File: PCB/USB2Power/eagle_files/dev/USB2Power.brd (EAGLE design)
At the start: 12.5 x 20 mm, 7 parts, among them SW1 PCM12SMTR

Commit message: USB2Power board components placed and ready for routing.
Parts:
- moved SW1 7.02 mm to (2.00, 8.50), flipped to the top, turned to 270 degrees
- moved C1 6.92 mm to (7.99, 4.50), flipped to the bottom, turned to 180 degrees
- moved C2 4.63 mm to (5.00, 11.0), flipped to the bottom, turned to 270 degrees
- moved USB1 4.51 mm to (8.50, 2.25)
- moved JP1 3.25 mm to (2.00, 14.8)
- moved L1 2.64 mm to (7.75, 11.2), flipped to the bottom
- moved VR1 2.20 mm to (7.25, 7.50), flipped to the bottom
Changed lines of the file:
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@@
 </autorouter>
 <elements>
-<element name="C1" library="SparkFun-Capacitors" package="0603-CAP" value="" x="1.75" y="7.5" smashed="yes" rot="R270">
-<attribute name="NAME" x="2.531" y="9.442" size="0.4064" layer="25" font="vector"/>
-<attribute name="VALUE" x="0.607" y="8.516" size="0.4064" layer="27" font="vector" rot="R270"/>
+<element name="C1" library="SparkFun-Capacitors" package="0603-CAP" value="" x="7.99" y="4.5" smashed="yes" rot="MR180">
+<attribute name="NAME" x="5.711" y="3.318" size="0.4064" layer="26" font="vector" rot="MR180"/>
+<attribute name="VALUE" x="6.974" y="5.643" size="0.4064" layer="28" font="vector" rot="MR180"/>
 </element>
-<element name="C2" library="SparkFun-Capacitors" package="0603-CAP" value="" x="2.53" y="14.92" smashed="yes">
-<attribute name="NAME" x="0.721" y="13.252" size="0.4064" layer="25" font="vector"/>
-<attribute name="VALUE" x="1.514" y="13.777" size="0.4064" layer="27" font="vector"/>
+<element name="C2" library="SparkFun-Capacitors" package="0603-CAP" value="" x="5" y="11" smashed="yes" rot="MR270">
+<attribute name="NAME" x="4.021" y="13.058" size="0.4064" layer="26" font="vector" rot="MR180"/>
+<attribute name="VALUE" x="6.143" y="12.016" size="0.4064" layer="28" font="vector" rot="MR270"/>
 </element>
-<element name="JP1" library="SparkFun-Connectors" package="1X04" value="" x="2" y="18" smashed="yes">
-<attribute name="NAME" x="9.5038" y="14.7588" size="1.27" layer="25" ratio="10"/>
-<attribute name="VALUE" x="0.73" y="14.825" size="1.27" layer="27"/>
+<element name="JP1" library="SparkFun-Connectors" package="1X04" value="" x="2" y="14.75" smashed="yes">
+<attribute name="NAME" x="8.4538" y="11.7588" size="1.27" layer="25" ratio="10"/>
+<attribute name="VALUE" x="0.73" y="11.575" size="1.27" layer="27"/>
 </element>
-<element name="L1" library="SparkFun-Passives" package="0603" value="" x="5.37" y="12.39" smashed="yes">
-<attribute name="PROD_ID" value="RES-07859" x="5.37" y="12.39" size="1.778" layer="27" display="off"/>
-<attribute name="NAME" x="7.191" y="12.442" size="0.4064" layer="25" font="vector"/>
-<attribute name="VALUE" x="4.354" y="11.247" size="0.4064" layer="27" font="vector"/>
+<element name="L1" library="SparkFun-Passives" package="0603" value="" x="7.75" y="11.25" smashed="yes" rot="MR0">
+<attribute name="PROD_ID" value="RES-07859" x="7.75" y="11.25" size="1.778" layer="28" rot="MR0" display="off"/>
+<attribute name="NAME" x="8.809" y="12.452" size="0.4064" layer="26" font="vector" rot="MR0"/>
+<attribute name="VALUE" x="8.766" y="10.107" size="0.4064" layer="28" font="vector" rot="MR0"/>
 </element>
-<element name="SW1" library="freddyLibr" package="PCM12SMTR" value="PCM12SMTR" x="4.67" y="2.01" smashed="yes" rot="MR0">
-<attribute name="NAME" x="6.24" y="5.13" size="1.27" layer="26" rot="MR0"/>
+<element name="SW1" library="freddyLibr" package="PCM12SMTR" value="PCM12SMTR" x="2" y="8.5" smashed="yes" rot="R270">
+<attribute name="NAME" x="0.53" y="2.72" size="1.27" layer="25"/>
 </element>
-<element name="USB1" library="freddyLibr" package="USB-MICROB-SMT" value="USB-MICROB-SMT5-PIN" x="4" y="2.5" smashed="yes">
-<attribute name="NAME" x="11.35" y="6.14" size="1.27" layer="25" rot="R180"/>
+<element name="USB1" library="freddyLibr" package="USB-MICROB-SMT" value="USB-MICROB-SMT5-PIN" x="8.5" y="2.25" smashed="yes">
+<attribute name="NAME" x="0.64" y="0.48" size="1.27" layer="25"/>
 </element>
-<element name="VR1" library="freddyLibr" package="UJ-5_TSOT" value="" x="5.3" y="8.51" smashed="yes">
-<attribute name="NAME" x="7.63" y="9.02" size="1.27" layer="25"/>
+<element name="VR1" library="freddyLibr" package="UJ-5_TSOT" value="" x="7.25" y="7.5" smashed="yes" rot="MR0">
+<attribute name="NAME" x="5.59" y="7.72" size="1.27" layer="26" rot="MR0"/>
 </element>
 </elements>
@@
 <contactref element="VR1" pad="3"/>
 <contactref element="C1" pad="2"/>
-<wire x1="6.25" y1="7.36" x2="2.42" y2="3.76" width="0" layer="19" extent="1-1"/>
-<wire x1="4.35" y1="7.36" x2="6.25" y2="7.36" width="0" layer="19" extent="1-1"/>
-<wire x1="1.75" y1="6.65" x2="4.35" y2="7.36" width="0" layer="19" extent="1-1"/>
+<wire x1="8.2" y1="6.35" x2="6.3" y2="6.35" width="0" layer="19" extent="1-1"/>
+<wire x1="8.84" y1="4.5" x2="8.2" y2="6.35" width="0" layer="19" extent="1-1"/>
+<wire x1="3.75" y1="6.25" x2="6.3" y2="6.35" width="0" layer="19" extent="1-16"/>
 </signal>
 <signal name="N$2">
 <contactref element="VR1" pad="4"/>
 <contactref element="L1" pad="1"/>
-<wire x1="4.52" y1="12.39" x2="4.35" y2="9.66" width="0" layer="19" extent="1-1"/>
+<wire x1="8.2" y1="8.65" x2="8.6" y2="11.25" width="0" layer="19" extent="1-16"/>
 </signal>
 <signal name="GND">
@@
 <contactref element="USB1" pad="9"/>
 <contactref element="JP1" pad="1"/>
-<wire x1="5.3" y1="7.36" x2="5.3" y2="4.13" width="0" layer="19" extent="1-1"/>
-<wire x1="2" y1="18" x2="5.3" y2="7.36" width="0" layer="19" extent="1-1"/>
-<wire x1="1.68" y1="14.92" x2="2" y2="18" width="0" layer="19" extent="1-1"/>
-<wire x1="1.75" y1="8.35" x2="1.68" y2="14.92" width="0" layer="19" extent="1-1"/>
+<wire x1="5" y1="11.85" x2="2" y2="14.75" width="0" layer="19" extent="16-16"/>
+<wire x1="7.14" y1="4.5" x2="5" y2="11.85" width="0" layer="19" extent="1-16"/>
+<wire x1="7.25" y1="6.35" x2="7.14" y2="4.5" width="0" layer="19" extent="1-1"/>
+<wire x1="9.8" y1="3.88" x2="7.25" y2="6.35" width="0" layer="19" extent="1-1"/>
 </signal>
 <signal name="VIN">
 <contactref element="USB1" pad="5"/>
 <contactref element="SW1" pad="2"/>
-<wire x1="3.92" y1="3.76" x2="2.7" y2="4.13" width="0" layer="19" extent="1-1"/>
+<wire x1="7.2" y1="3.88" x2="3.75" y2="7.75" width="0" layer="19" extent="1-16"/>
 </signal>
 <signal name="VOUT">
@@
 <contactref element="SW1" pad="1"/>
 <contactref element="JP1" pad="2"/>
-<wire x1="6.22" y1="12.39" x2="3.38" y2="14.92" width="0" layer="19" extent="1-1"/>
-<wire x1="4.54" y1="18" x2="6.22" y2="12.39" width="0" layer="19" extent="1-1"/>
-<wire x1="6.92" y1="3.76" x2="4.54" y2="18" width="0" layer="19" extent="1-1"/>
-<wire x1="6.25" y1="9.66" x2="6.22" y2="12.39" width="0" layer="19" extent="1-1"/>
+<wire x1="6.3" y1="8.65" x2="6.9" y2="11.25" width="0" layer="19" extent="1-16"/>
+<wire x1="4.54" y1="14.75" x2="6.9" y2="11.25" width="0" layer="19" extent="16-16"/>
+<wire x1="5" y1="10.15" x2="6.3" y2="8.65" width="0" layer="19" extent="1-16"/>
+<wire x1="3.75" y1="10.75" x2="5" y2="10.15" width="0" layer="19" extent="16-16"/>
 </signal>
 </signals>

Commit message: Slightly tweak borders of USB2Power.
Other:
- board size 12.5 x 20 mm -> 12.5 x 16.5 mm
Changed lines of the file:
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@@
 <plain>
 <wire x1="0" y1="0" x2="12.5" y2="0" width="0" layer="20"/>
-<wire x1="12.5" y1="0" x2="12.52" y2="20" width="0" layer="20"/>
-<wire x1="12.52" y1="20" x2="0" y2="20" width="0" layer="20"/>
-<wire x1="0" y1="20" x2="0" y2="0" width="0" layer="20"/>
+<wire x1="12.5" y1="0" x2="12.5" y2="16.5" width="0" layer="20"/>
+<wire x1="12.5" y1="16.5" x2="0" y2="16.5" width="0" layer="20"/>
+<wire x1="0" y1="16.5" x2="0" y2="0" width="0" layer="20"/>
 </plain>
 <attributes>

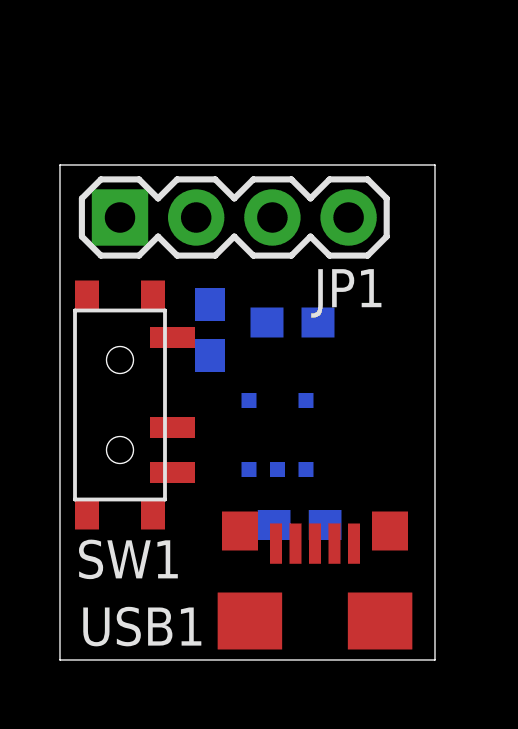
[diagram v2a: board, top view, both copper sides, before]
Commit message: All connected up. Also added ground for the other two header pins as opposed to NC. Made connections a little better. Some known DRC failures.
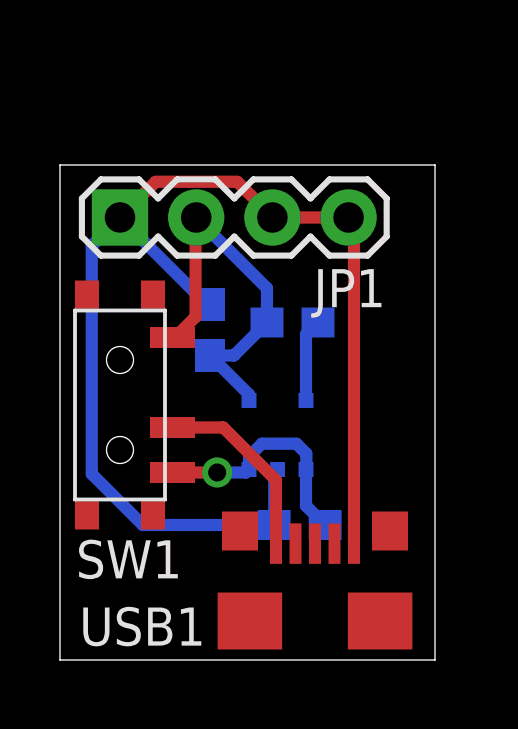
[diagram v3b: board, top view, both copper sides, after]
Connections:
- net GND: now also JP1.3, JP1.4
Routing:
- net GND: track 0.00 -> 41.4 mm
- net VOUT: track 0.00 -> 13.2 mm
- net N$1: track 0.00 -> 7.90 mm, vias 0 -> 1
- net VIN: track 0.00 -> 6.29 mm
- net N$2: track 0.00 -> 2.77 mm
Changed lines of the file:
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@@
 <contactref element="VR1" pad="3"/>
 <contactref element="C1" pad="2"/>
-<wire x1="8.2" y1="6.35" x2="6.3" y2="6.35" width="0" layer="19" extent="1-1"/>
-<wire x1="8.84" y1="4.5" x2="8.2" y2="6.35" width="0" layer="19" extent="1-1"/>
-<wire x1="3.75" y1="6.25" x2="6.3" y2="6.35" width="0" layer="19" extent="1-16"/>
+<wire x1="3.75" y1="6.25" x2="5.24" y2="6.25" width="0.4064" layer="1"/>
+<via x="5.24" y="6.25" extent="1-16" drill="0.6"/>
+<wire x1="5.24" y1="6.25" x2="6.2" y2="6.25" width="0.4064" layer="16"/>
+<wire x1="6.2" y1="6.25" x2="6.3" y2="6.35" width="0.4064" layer="16"/>
+<wire x1="8.2" y1="6.35" x2="8.2" y2="5.14" width="0.4064" layer="16"/>
+<wire x1="8.2" y1="5.14" x2="8.84" y2="4.5" width="0.4064" layer="16"/>
+<wire x1="6.3" y1="6.35" x2="6.3" y2="6.78" width="0.4064" layer="16"/>
+<wire x1="6.3" y1="6.78" x2="6.73" y2="7.21" width="0.4064" layer="16"/>
+<wire x1="6.73" y1="7.21" x2="7.88" y2="7.21" width="0.4064" layer="16"/>
+<wire x1="7.88" y1="7.21" x2="8.21" y2="6.88" width="0.4064" layer="16"/>
+<wire x1="8.21" y1="6.88" x2="8.21" y2="6.36" width="0.4064" layer="16"/>
+<wire x1="8.21" y1="6.36" x2="8.2" y2="6.35" width="0.4064" layer="16"/>
 </signal>
 <signal name="N$2">
 <contactref element="VR1" pad="4"/>
 <contactref element="L1" pad="1"/>
-<wire x1="8.2" y1="8.65" x2="8.6" y2="11.25" width="0" layer="19" extent="1-16"/>
+<wire x1="8.2" y1="8.65" x2="8.2" y2="10.85" width="0.4064" layer="16"/>
+<wire x1="8.2" y1="10.85" x2="8.6" y2="11.25" width="0.4064" layer="16"/>
 </signal>
 <signal name="GND">
@@
 <contactref element="USB1" pad="9"/>
 <contactref element="JP1" pad="1"/>
-<wire x1="5" y1="11.85" x2="2" y2="14.75" width="0" layer="19" extent="16-16"/>
-<wire x1="7.14" y1="4.5" x2="5" y2="11.85" width="0" layer="19" extent="1-16"/>
-<wire x1="7.25" y1="6.35" x2="7.14" y2="4.5" width="0" layer="19" extent="1-1"/>
-<wire x1="9.8" y1="3.88" x2="7.25" y2="6.35" width="0" layer="19" extent="1-1"/>
+<contactref element="JP1" pad="4"/>
+<contactref element="JP1" pad="3"/>
+<wire x1="9.8" y1="3.88" x2="9.8" y2="14.57" width="0.4064" layer="1"/>
+<wire x1="9.8" y1="14.57" x2="9.62" y2="14.75" width="0.4064" layer="1"/>
+<wire x1="9.62" y1="14.75" x2="7.08" y2="14.75" width="0.4064" layer="1"/>
+<wire x1="7.08" y1="14.75" x2="7.08" y2="14.77" width="0.4064" layer="1"/>
+<wire x1="7.08" y1="14.77" x2="5.91" y2="15.94" width="0.4064" layer="1"/>
+<wire x1="5.91" y1="15.94" x2="3.19" y2="15.94" width="0.4064" layer="1"/>
+<wire x1="3.19" y1="15.94" x2="2" y2="14.75" width="0.4064" layer="1"/>
+<wire x1="7.14" y1="4.5" x2="7.14" y2="6.24" width="0.4064" layer="16"/>
+<wire x1="7.14" y1="6.24" x2="7.25" y2="6.35" width="0.4064" layer="16"/>
+<wire x1="5" y1="11.85" x2="4.9" y2="11.85" width="0.4064" layer="16"/>
+<wire x1="4.9" y1="11.85" x2="2" y2="14.75" width="0.4064" layer="16"/>
+<wire x1="7.14" y1="4.5" x2="2.76" y2="4.5" width="0.4064" layer="16"/>
+<wire x1="2.76" y1="4.5" x2="1.06" y2="6.2" width="0.4064" layer="16"/>
+<wire x1="1.06" y1="6.2" x2="1.06" y2="13.81" width="0.4064" layer="16"/>
+<wire x1="1.06" y1="13.81" x2="2" y2="14.75" width="0.4064" layer="16"/>
 </signal>
 <signal name="VIN">
 <contactref element="USB1" pad="5"/>
 <contactref element="SW1" pad="2"/>
-<wire x1="7.2" y1="3.88" x2="3.75" y2="7.75" width="0" layer="19" extent="1-16"/>
+<wire x1="7.2" y1="3.88" x2="7.2" y2="5.99" width="0.4064" layer="1"/>
+<wire x1="7.2" y1="5.99" x2="5.44" y2="7.75" width="0.4064" layer="1"/>
+<wire x1="5.44" y1="7.75" x2="3.75" y2="7.75" width="0.4064" layer="1"/>
 </signal>
 <signal name="VOUT">
@@
 <contactref element="SW1" pad="1"/>
 <contactref element="JP1" pad="2"/>
-<wire x1="6.3" y1="8.65" x2="6.9" y2="11.25" width="0" layer="19" extent="1-16"/>
-<wire x1="4.54" y1="14.75" x2="6.9" y2="11.25" width="0" layer="19" extent="16-16"/>
-<wire x1="5" y1="10.15" x2="6.3" y2="8.65" width="0" layer="19" extent="1-16"/>
-<wire x1="3.75" y1="10.75" x2="5" y2="10.15" width="0" layer="19" extent="16-16"/>
+<wire x1="3.75" y1="10.75" x2="3.83" y2="10.75" width="0.4064" layer="1"/>
+<wire x1="3.83" y1="10.75" x2="4.52" y2="11.44" width="0.4064" layer="1"/>
+<wire x1="4.52" y1="11.44" x2="4.52" y2="14.73" width="0.4064" layer="1"/>
+<wire x1="4.52" y1="14.73" x2="4.54" y2="14.75" width="0.4064" layer="1"/>
+<wire x1="6.3" y1="8.65" x2="6.3" y2="8.85" width="0.4064" layer="16"/>
+<wire x1="6.3" y1="8.85" x2="5" y2="10.15" width="0.4064" layer="16"/>
+<wire x1="6.9" y1="11.25" x2="6.9" y2="12.39" width="0.4064" layer="16"/>
+<wire x1="6.9" y1="12.39" x2="4.54" y2="14.75" width="0.4064" layer="16"/>
+<wire x1="5" y1="10.15" x2="5.8" y2="10.15" width="0.4064" layer="16"/>
+<wire x1="5.8" y1="10.15" x2="6.9" y2="11.25" width="0.4064" layer="16"/>
 </signal>
 </signals>
